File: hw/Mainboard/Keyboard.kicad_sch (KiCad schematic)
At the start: 8 parts, among them J15 KEYBOARD_EX, J2 KEYBOARD, U1 74LS145

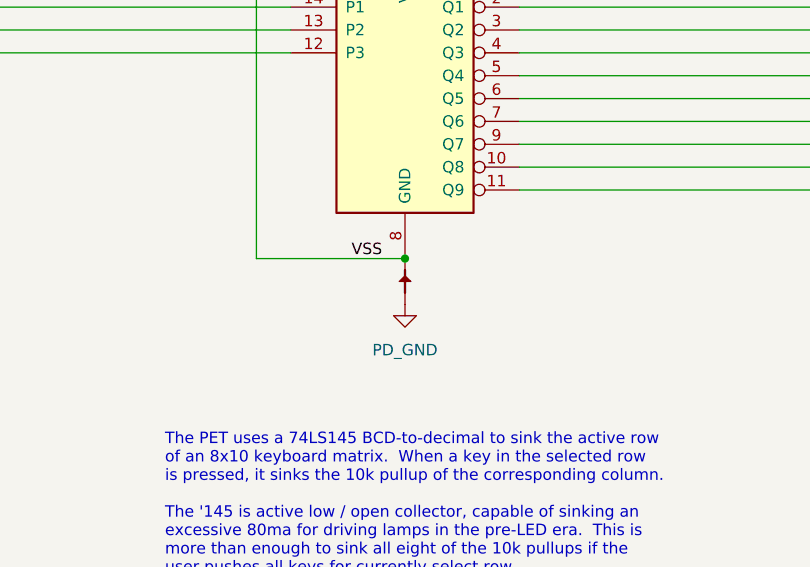
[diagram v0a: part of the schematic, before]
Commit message: hw: stitched copper planes (wip)
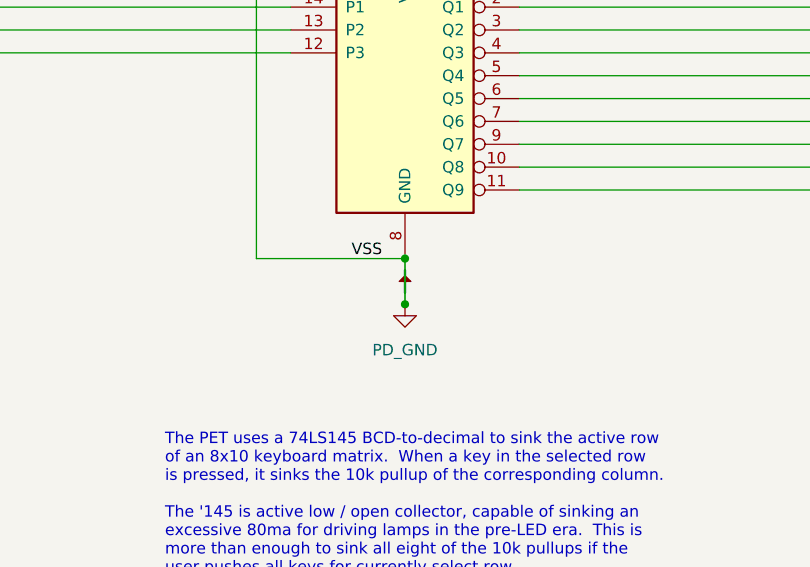
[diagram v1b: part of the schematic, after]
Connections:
- net VSS is gone; now on net PD_GND: C1.2, J15.7 (Pin_7), PT33.2, U1.8 (GND)
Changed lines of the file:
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@@
   (junction (at 152.4 50.8) (diameter 0) (color 0 0 0 0)
   )
+  (junction (at 110.49 104.14) (diameter 0) (color 0 0 0 0)
+  )
   (junction (at 149.86 48.26) (diameter 0) (color 0 0 0 0)
   )
@@
   )
   (wire (pts (xy 135.89 60.96) (xy 170.18 60.96))
+    (stroke (width 0) (type default) (color 0 0 0 0))
+  )
+  (wire (pts (xy 110.49 99.06) (xy 110.49 104.14))
     (stroke (width 0) (type default) (color 0 0 0 0))
   )
@@
       (effects (font (size 1.27 1.27)) hide)
     )
-    (property "Datasheet" "https://cdn.amphenol-cs.com/media/wysiwyg/files/documentation/datasheet/boardwiretoboard/bwb_econostik_254headers.pdf" (id 3) (at 201.93 73.66 0)
+    (property "Datasheet" "" (id 3) (at 201.93 73.66 0)
       (effects (font (size 1.27 1.27)) hide)
     )

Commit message: hw: add more Mouse part numbers
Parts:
- J15: MOUSER (none) -> 649-1012938195002BLF
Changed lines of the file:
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@@
+      (effects (font (size 1.27 1.27)) hide)
+    )
+    (property "MOUSER" "649-1012938195002BLF" (id 4) (at 199.39 135.89 0)
       (effects (font (size 1.27 1.27)) hide)
     )

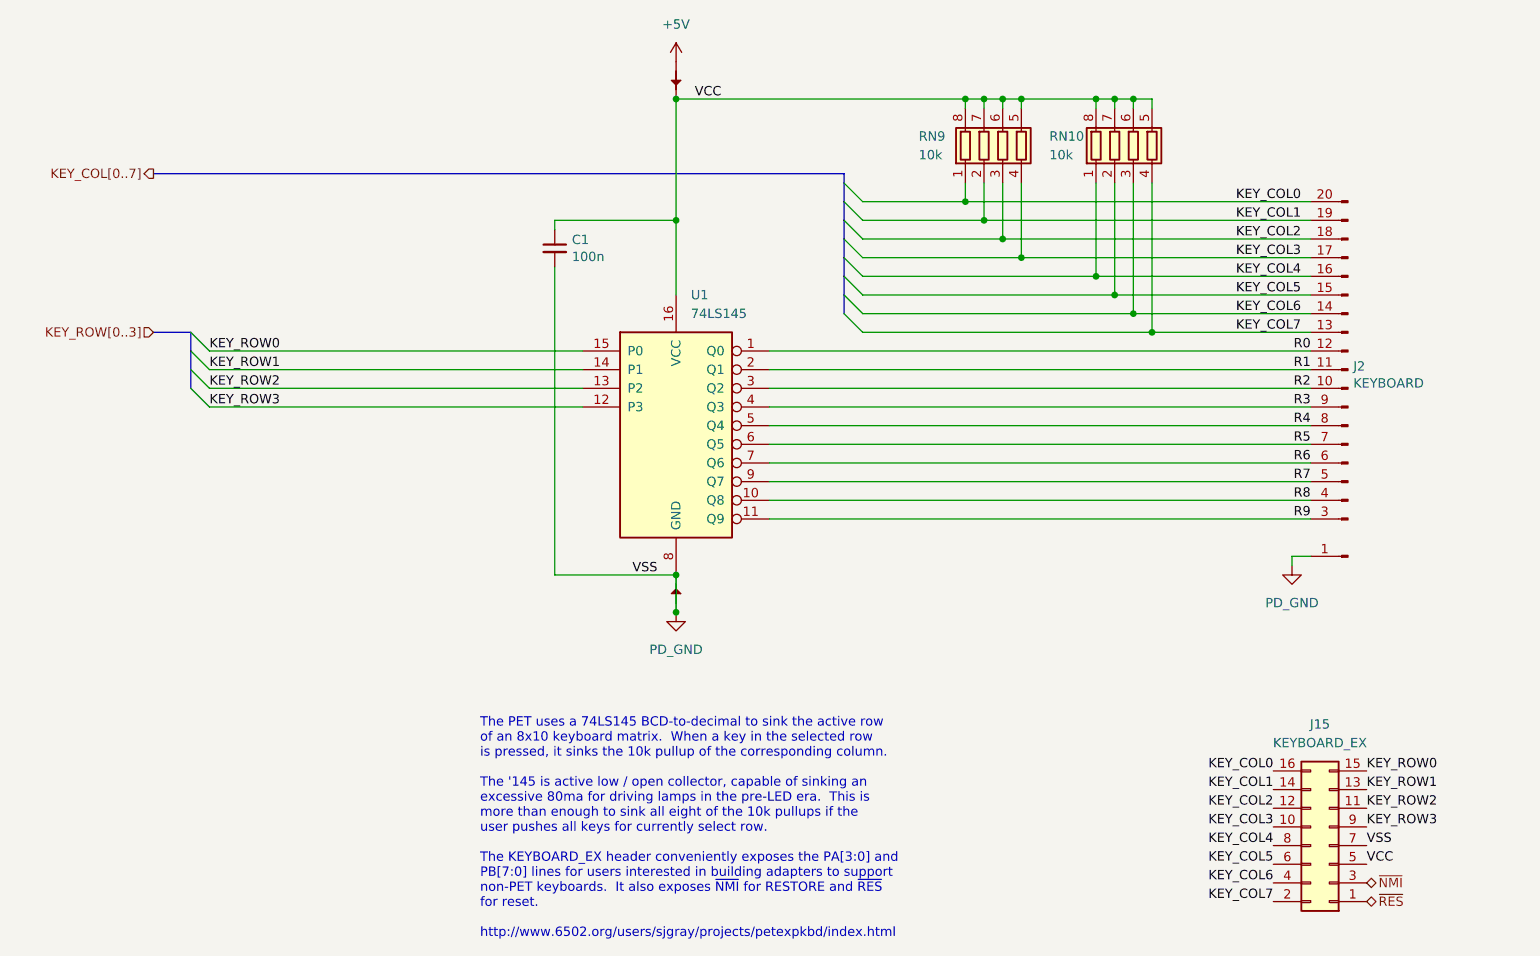
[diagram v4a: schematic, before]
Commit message: hw: 9V DC plug on left edge, change default track size
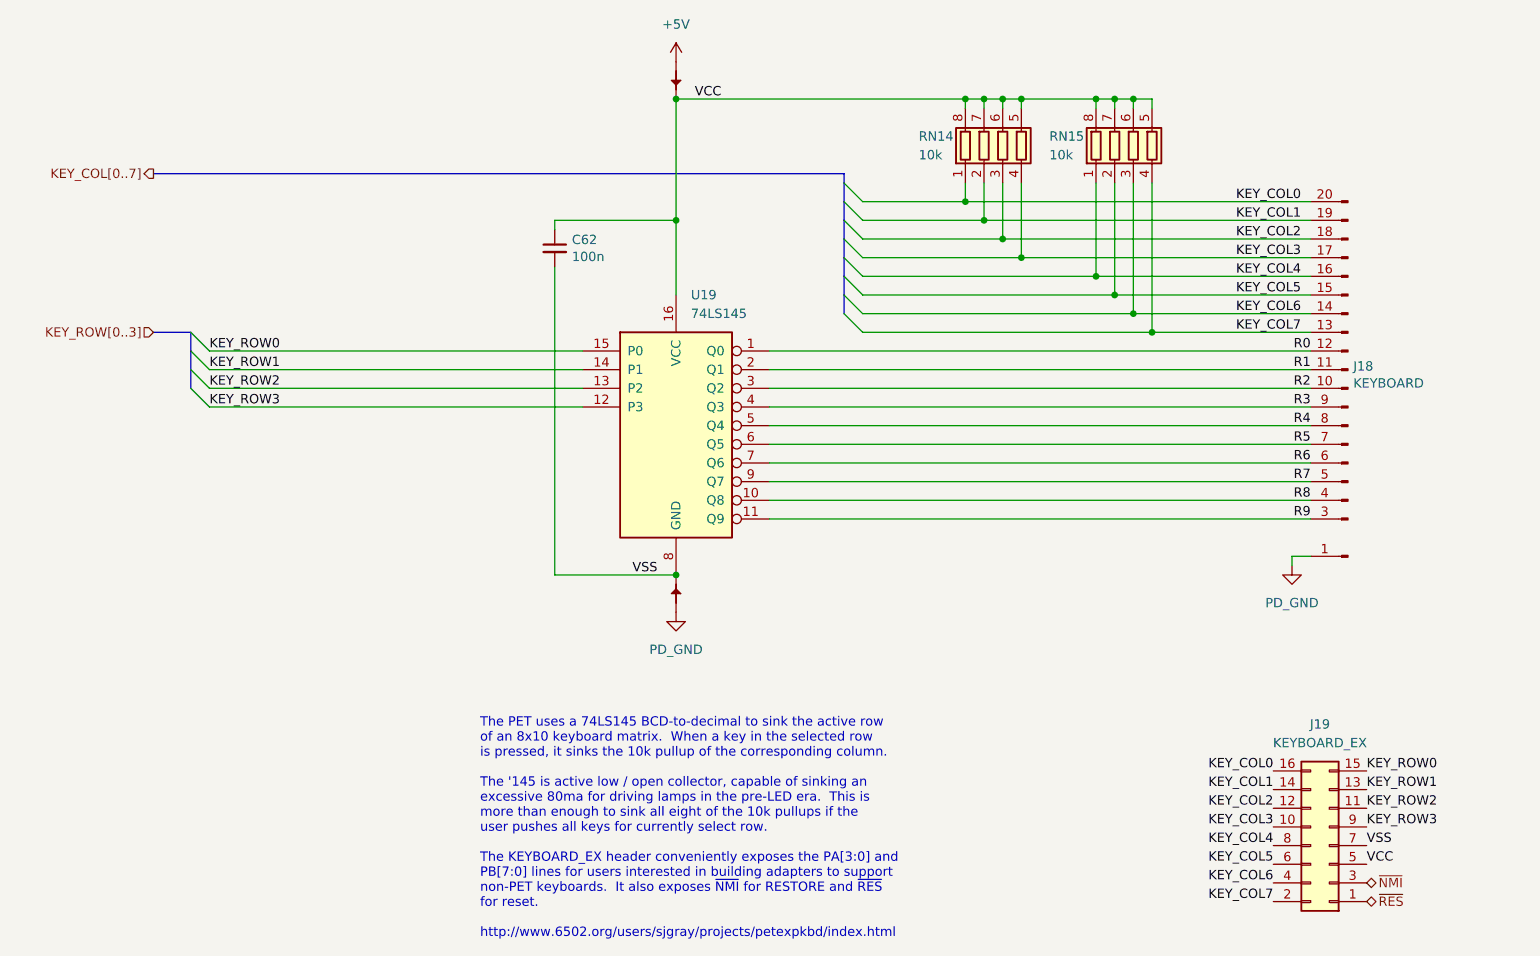
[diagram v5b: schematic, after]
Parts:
- renumbered C1 to C62, J2 to J18, J15 to J19, PT17 to PT42, PT33 to PT43, RN9 to RN14, RN10 to RN15, U1 to U19
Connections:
- net PD_GND: no longer C62.2, J19.7 (Pin_7), PT43.2, U19.8 (GND)
- new net VSS: C62.2, J19.7 (Pin_7), PT43.2, U19.8 (GND)
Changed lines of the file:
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@@
   (junction (at 152.4 50.8) (diameter 0) (color 0 0 0 0)
   )
-  (junction (at 110.49 104.14) (diameter 0) (color 0 0 0 0)
-  )
   (junction (at 149.86 48.26) (diameter 0) (color 0 0 0 0)
   )
@@
   )
   (wire (pts (xy 135.89 60.96) (xy 170.18 60.96))
-    (stroke (width 0) (type default) (color 0 0 0 0))
-  )
-  (wire (pts (xy 110.49 99.06) (xy 110.49 104.14))
     (stroke (width 0) (type default) (color 0 0 0 0))
   )
@@
   (symbol (lib_id "Retrocomputing:CBM_PET_Keyboard_Conn_Keyed_20P") (at 201.93 73.66 180) (unit 1)
     (in_bom yes) (on_board yes)
-    (property "Reference" "J2" (id 0) (at 202.6412 70.6628 0)
+    (property "Reference" "J18" (id 0) (at 202.6412 70.6628 0)
       (effects (font (size 1.27 1.27)) (justify right))
     )
@@
   (symbol (lib_id "Device:C_Small") (at 93.98 54.61 0) (unit 1)
     (in_bom yes) (on_board yes)
-    (property "Reference" "C1" (id 0) (at 96.3168 53.4416 0)
+    (property "Reference" "C62" (id 0) (at 96.3168 53.4416 0)
       (effects (font (size 1.27 1.27)) (justify left))
     )
@@
   (symbol (lib_id "PET:PowerTie_2") (at 110.49 31.75 270) (unit 1)
     (in_bom yes) (on_board yes) (fields_autoplaced)
-    (property "Reference" "PT17" (id 0) (at 112.395 31.75 0)
+    (property "Reference" "PT42" (id 0) (at 112.395 31.75 0)
       (effects (font (size 1.27 1.27)) hide)
     )
@@
   (symbol (lib_id "PET:PD_GND") (at 110.49 104.14 0) (unit 1)
     (in_bom yes) (on_board yes) (fields_autoplaced)
-    (property "Reference" "#PWR0133" (id 0) (at 110.49 110.49 0)
+    (property "Reference" "#PWR0119" (id 0) (at 110.49 110.49 0)
       (effects (font (size 1.27 1.27)) hide)
     )
@@
   (symbol (lib_id "74xx:74LS145") (at 110.49 78.74 0) (unit 1)
     (in_bom yes) (on_board yes)
-    (property "Reference" "U1" (id 0) (at 112.5094 60.96 0)
+    (property "Reference" "U19" (id 0) (at 112.5094 60.96 0)
       (effects (font (size 1.27 1.27)) (justify left))
     )
@@
   (symbol (lib_id "Connector_Generic:Conn_02x08_Odd_Even") (at 199.39 135.89 180) (unit 1)
     (in_bom yes) (on_board yes) (fields_autoplaced)
-    (property "Reference" "J15" (id 0) (at 198.12 119.38 0))
+    (property "Reference" "J19" (id 0) (at 198.12 119.38 0))
     (property "Value" "KEYBOARD_EX" (id 1) (at 198.12 121.92 0))
     (property "Footprint" "Connector_PinHeader_2.54mm:PinHeader_2x08_P2.54mm_Vertical" (id 2) (at 199.39 135.89 0)
@@
   (symbol (lib_id "PET:PD_GND") (at 194.31 97.79 0) (unit 1)
     (in_bom yes) (on_board yes) (fields_autoplaced)
-    (property "Reference" "#PWR0182" (id 0) (at 194.31 104.14 0)
+    (property "Reference" "#PWR0118" (id 0) (at 194.31 104.14 0)
       (effects (font (size 1.27 1.27)) hide)
     )
@@
   (symbol (lib_id "power:+5V") (at 110.49 29.21 0) (unit 1)
     (in_bom yes) (on_board yes) (fields_autoplaced)
-    (property "Reference" "#PWR0132" (id 0) (at 110.49 33.02 0)
+    (property "Reference" "#PWR0117" (id 0) (at 110.49 33.02 0)
       (effects (font (size 1.27 1.27)) hide)
     )
@@
   (symbol (lib_id "PET:PowerTie_2") (at 110.49 101.6 270) (mirror x) (unit 1)
     (in_bom yes) (on_board yes) (fields_autoplaced)
-    (property "Reference" "PT33" (id 0) (at 112.395 101.6 0)
+    (property "Reference" "PT43" (id 0) (at 112.395 101.6 0)
       (effects (font (size 1.27 1.27)) hide)
     )
@@
   (symbol (lib_id "Device:R_Pack04") (at 154.94 40.64 0) (unit 1)
     (in_bom yes) (on_board yes)
-    (property "Reference" "RN9" (id 0) (at 143.51 39.37 0)
+    (property "Reference" "RN14" (id 0) (at 143.51 39.37 0)
       (effects (font (size 1.27 1.27)) (justify left))
     )
@@
   (symbol (lib_id "Device:R_Pack04") (at 172.72 40.64 0) (unit 1)
     (in_bom yes) (on_board yes)
-    (property "Reference" "RN10" (id 0) (at 161.29 39.37 0)
+    (property "Reference" "RN15" (id 0) (at 161.29 39.37 0)
       (effects (font (size 1.27 1.27)) (justify left))
     )

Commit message: hw: 25x2 header (wip)
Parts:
- renumbered J18 to J19, J19 to J20
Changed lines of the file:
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@@
   (symbol (lib_id "Retrocomputing:CBM_PET_Keyboard_Conn_Keyed_20P") (at 201.93 73.66 180) (unit 1)
     (in_bom yes) (on_board yes)
-    (property "Reference" "J18" (id 0) (at 202.6412 70.6628 0)
+    (property "Reference" "J19" (id 0) (at 202.6412 70.6628 0)
       (effects (font (size 1.27 1.27)) (justify right))
     )
@@
   (symbol (lib_id "PET:PD_GND") (at 110.49 104.14 0) (unit 1)
     (in_bom yes) (on_board yes) (fields_autoplaced)
-    (property "Reference" "#PWR0119" (id 0) (at 110.49 110.49 0)
+    (property "Reference" "#PWR0121" (id 0) (at 110.49 110.49 0)
       (effects (font (size 1.27 1.27)) hide)
     )
@@
   (symbol (lib_id "Connector_Generic:Conn_02x08_Odd_Even") (at 199.39 135.89 180) (unit 1)
     (in_bom yes) (on_board yes) (fields_autoplaced)
-    (property "Reference" "J19" (id 0) (at 198.12 119.38 0))
+    (property "Reference" "J20" (id 0) (at 198.12 119.38 0))
     (property "Value" "KEYBOARD_EX" (id 1) (at 198.12 121.92 0))
     (property "Footprint" "Connector_PinHeader_2.54mm:PinHeader_2x08_P2.54mm_Vertical" (id 2) (at 199.39 135.89 0)
@@
   (symbol (lib_id "PET:PD_GND") (at 194.31 97.79 0) (unit 1)
     (in_bom yes) (on_board yes) (fields_autoplaced)
-    (property "Reference" "#PWR0118" (id 0) (at 194.31 104.14 0)
+    (property "Reference" "#PWR0120" (id 0) (at 194.31 104.14 0)
       (effects (font (size 1.27 1.27)) hide)
     )
@@
   (symbol (lib_id "power:+5V") (at 110.49 29.21 0) (unit 1)
     (in_bom yes) (on_board yes) (fields_autoplaced)
-    (property "Reference" "#PWR0117" (id 0) (at 110.49 33.02 0)
+    (property "Reference" "#PWR0119" (id 0) (at 110.49 33.02 0)
       (effects (font (size 1.27 1.27)) hide)
     )

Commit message: hw: 2x config switch (wip)
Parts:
- renumbered J19 to J18, J20 to J19
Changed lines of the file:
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@@
   (symbol (lib_id "Retrocomputing:CBM_PET_Keyboard_Conn_Keyed_20P") (at 201.93 73.66 180) (unit 1)
     (in_bom yes) (on_board yes)
-    (property "Reference" "J19" (id 0) (at 202.6412 70.6628 0)
+    (property "Reference" "J18" (id 0) (at 202.6412 70.6628 0)
       (effects (font (size 1.27 1.27)) (justify right))
     )
@@
   (symbol (lib_id "PET:PD_GND") (at 110.49 104.14 0) (unit 1)
     (in_bom yes) (on_board yes) (fields_autoplaced)
-    (property "Reference" "#PWR0121" (id 0) (at 110.49 110.49 0)
+    (property "Reference" "#PWR0127" (id 0) (at 110.49 110.49 0)
       (effects (font (size 1.27 1.27)) hide)
     )
@@
   (symbol (lib_id "Connector_Generic:Conn_02x08_Odd_Even") (at 199.39 135.89 180) (unit 1)
     (in_bom yes) (on_board yes) (fields_autoplaced)
-    (property "Reference" "J20" (id 0) (at 198.12 119.38 0))
+    (property "Reference" "J19" (id 0) (at 198.12 119.38 0))
     (property "Value" "KEYBOARD_EX" (id 1) (at 198.12 121.92 0))
     (property "Footprint" "Connector_PinHeader_2.54mm:PinHeader_2x08_P2.54mm_Vertical" (id 2) (at 199.39 135.89 0)
@@
   (symbol (lib_id "PET:PD_GND") (at 194.31 97.79 0) (unit 1)
     (in_bom yes) (on_board yes) (fields_autoplaced)
-    (property "Reference" "#PWR0120" (id 0) (at 194.31 104.14 0)
+    (property "Reference" "#PWR0126" (id 0) (at 194.31 104.14 0)
       (effects (font (size 1.27 1.27)) hide)
     )
@@
   (symbol (lib_id "power:+5V") (at 110.49 29.21 0) (unit 1)
     (in_bom yes) (on_board yes) (fields_autoplaced)
-    (property "Reference" "#PWR0119" (id 0) (at 110.49 33.02 0)
+    (property "Reference" "#PWR0125" (id 0) (at 110.49 33.02 0)
       (effects (font (size 1.27 1.27)) hide)
     )
